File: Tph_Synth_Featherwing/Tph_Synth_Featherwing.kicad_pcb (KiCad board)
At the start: 2 copper layers, 51 x 58.5 mm, 55 parts, among them J1 AudioJack3, J2 Conn_01x04, U1 PAM2401SCADJ, U2 LM2663M, U3 Opamp_Quad_Generic, U4 MCP4728

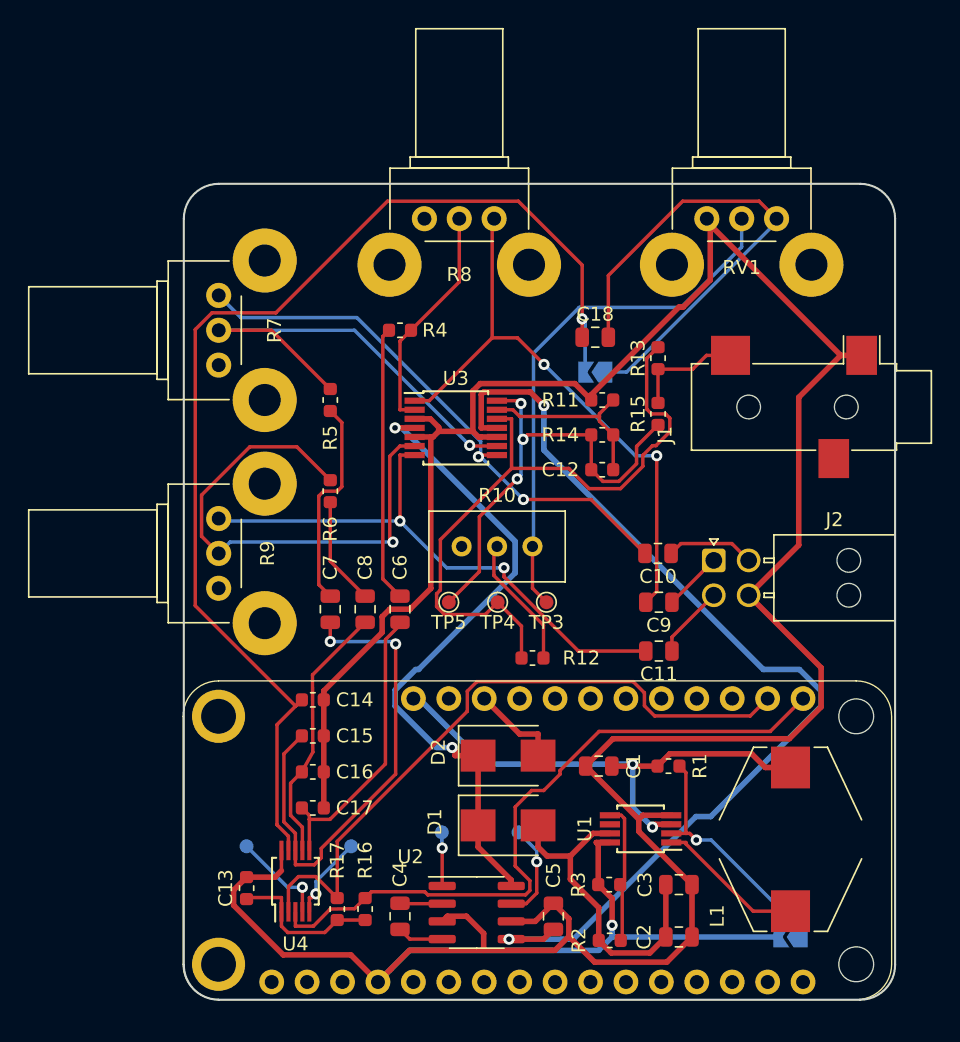
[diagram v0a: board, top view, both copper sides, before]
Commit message: Added ground pour and stitching vias
Signed-off-by: Tisham Dhar <whatnickd@gmail.com>
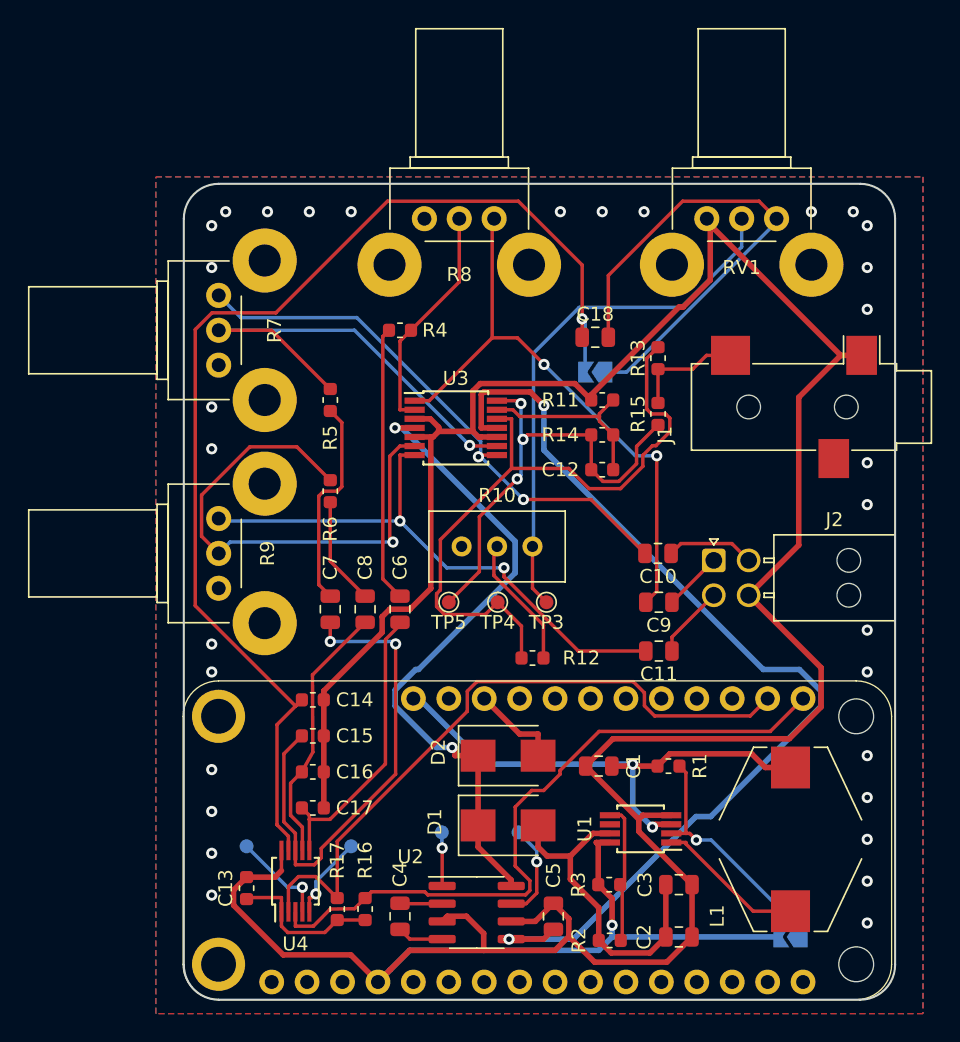
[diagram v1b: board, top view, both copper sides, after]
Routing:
- net GND: vias 1 -> 32
- added copper zone on B.Cu, net GND
- added copper zone on F.Cu, net GND
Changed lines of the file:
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@@
     (thickness 1.6)
     (drawings 8)
-    (tracks 446)
+    (tracks 477)
     (zones 0)
     (modules 55)
@@
   (gr_line (start 89.5 78) (end 135.5 78) (layer Edge.Cuts) (width 0.15))
   (gr_line (start 87 134) (end 87 80.5) (layer Edge.Cuts) (width 0.15))
+  (via (at 132 80) (size 0.8) (drill 0.4) (layers F.Cu B.Cu) (net 4))
+  (via (at 135 80) (size 0.8) (drill 0.4) (layers F.Cu B.Cu) (net 4))
+  (via (at 136 81) (size 0.8) (drill 0.4) (layers F.Cu B.Cu) (net 4))
+  (via (at 136 84) (size 0.8) (drill 0.4) (layers F.Cu B.Cu) (net 4))
+  (via (at 136 87) (size 0.8) (drill 0.4) (layers F.Cu B.Cu) (net 4))
+  (via (at 89 81) (size 0.8) (drill 0.4) (layers F.Cu B.Cu) (net 4))
+  (via (at 89 84) (size 0.8) (drill 0.4) (layers F.Cu B.Cu) (net 4))
+  (via (at 89 111) (size 0.8) (drill 0.4) (layers F.Cu B.Cu) (net 4))
+  (via (at 89 113) (size 0.8) (drill 0.4) (layers F.Cu B.Cu) (net 4))
+  (via (at 136 131) (size 0.8) (drill 0.4) (layers F.Cu B.Cu) (net 4))
+  (via (at 136 128) (size 0.8) (drill 0.4) (layers F.Cu B.Cu) (net 4))
+  (via (at 136 125) (size 0.8) (drill 0.4) (layers F.Cu B.Cu) (net 4))
+  (via (at 136 122) (size 0.8) (drill 0.4) (layers F.Cu B.Cu) (net 4))
+  (via (at 136 119) (size 0.8) (drill 0.4) (layers F.Cu B.Cu) (net 4))
+  (via (at 136 113) (size 0.8) (drill 0.4) (layers F.Cu B.Cu) (net 4))
+  (via (at 136 110) (size 0.8) (drill 0.4) (layers F.Cu B.Cu) (net 4))
+  (via (at 136 101) (size 0.8) (drill 0.4) (layers F.Cu B.Cu) (net 4))
+  (via (at 136 98) (size 0.8) (drill 0.4) (layers F.Cu B.Cu) (net 4))
+  (via (at 89 97) (size 0.8) (drill 0.4) (layers F.Cu B.Cu) (net 4))
+  (via (at 89 94) (size 0.8) (drill 0.4) (layers F.Cu B.Cu) (net 4))
+  (via (at 90 80) (size 0.8) (drill 0.4) (layers F.Cu B.Cu) (net 4))
+  (via (at 93 80) (size 0.8) (drill 0.4) (layers F.Cu B.Cu) (net 4))
+  (via (at 96 80) (size 0.8) (drill 0.4) (layers F.Cu B.Cu) (net 4))
+  (via (at 99 80) (size 0.8) (drill 0.4) (layers F.Cu B.Cu) (net 4))
+  (via (at 120 80) (size 0.8) (drill 0.4) (layers F.Cu B.Cu) (net 4))
+  (via (at 117 80) (size 0.8) (drill 0.4) (layers F.Cu B.Cu) (net 4))
+  (via (at 114 80) (size 0.8) (drill 0.4) (layers F.Cu B.Cu) (net 4))
+  (via (at 89 129) (size 0.8) (drill 0.4) (layers F.Cu B.Cu) (net 4))
+  (via (at 89 126) (size 0.8) (drill 0.4) (layers F.Cu B.Cu) (net 4))
+  (via (at 89 123) (size 0.8) (drill 0.4) (layers F.Cu B.Cu) (net 4))
+  (via (at 89 120) (size 0.8) (drill 0.4) (layers F.Cu B.Cu) (net 4))
   (segment (start 94 125.8) (end 94 127.25) (width 0.25) (layer F.Cu) (net 4))
   (segment (start 93.5375 127.7125) (end 94 127.25) (width 0.4) (layer F.Cu) (net 4))
@@
   (segment (start 116.3354 124.575) (end 117.55 124.575) (width 0.4) (layer F.Cu) (net 66))
   (segment (start 114.7134 126.197) (end 116.3354 124.575) (width 0.4) (layer F.Cu) (net 66))
+  (zone (net 4) (net_name GND) (layer F.Cu) (hatch edge 0.508)
+    (connect_pads (clearance 0.508))
+    (min_thickness 0.254)
+    (fill yes (arc_segments 16) (thermal_gap 0.508) (thermal_bridge_width 0.508))
+    (polygon
+      (pts
+        (xy 85 77.5) (xy 140 77.5) (xy 140 137.5) (xy 85 137.5)
+      )
+    )
+  )
+  (zone (net 4) (net_name GND) (layer B.Cu) (hatch edge 0.508)
+    (connect_pads (clearance 0.508))
+    (min_thickness 0.254)
+    (fill yes (arc_segments 16) (thermal_gap 0.508) (thermal_bridge_width 0.508))
+    (polygon
+      (pts
+        (xy 85 77.5) (xy 140 77.5) (xy 140 137.5) (xy 85 137.5)
+      )
+    )
+  )
 )

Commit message: Add blurb silk screen
Signed-off-by: Tisham Dhar <whatnickd@gmail.com>
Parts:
- added LOGO1: Logo_Open_Hardware_Small, Symbol:OSHW-Logo2_7.3x6mm_SilkScreen, B.Cu at (126.2, 123.5)
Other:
- board text added: "3-phase Simulator Featherwing. Suitable for use with Teensy Feather at around 3.2MHz I2C clock."
- board text added: "v0.1 20/12/2019 by Tisham (whatnick) Dhar OSHW TAPR"
